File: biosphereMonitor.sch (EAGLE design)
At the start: 58 parts, among them IC1 XMEGA32A4AU, IC2 LM35, IC3 FT232RL, IC4 NE555D, IC5 SST25VF040, Q1 16Mhz, Q2 32kHz

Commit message: placed Parts
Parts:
- added C19: 4,7µF, rcl:CPOL-EUE2-5
- added R15: 10k, rcl:R-EU_R0805
- D1: value LM4050 2.5 -> 2.5
- JP5: value (none) -> BAT
- PH1: value BPW 96C TEL -> BPW 96
- renumbered BT! to BT1
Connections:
- net D+ renamed D_P
- net D- renamed D_N
- net N$9 renamed AVCC
- net USB_MC_D+ renamed USB_MC_D_P
- net USB_MC_D- renamed USB_MC_D_N
- new net N$28: IC3.!RESET, R15.2
- net +3V3: now also C19.+, R15.1
- net GND: now also C19.-
- net N$5: now also Q2.1; no longer Q2.2
- net N$6: now also Q2.2; no longer Q2.1
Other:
- moved on the sheet: Q2

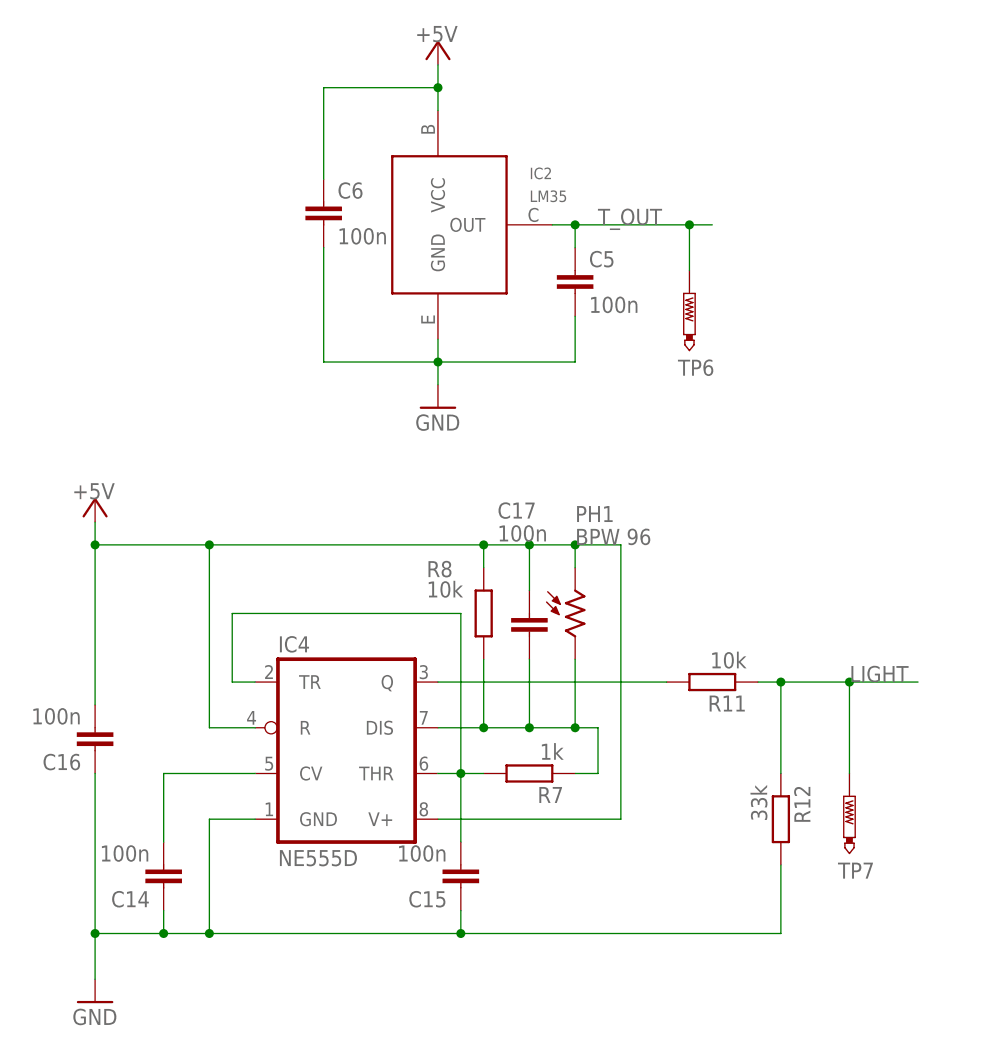
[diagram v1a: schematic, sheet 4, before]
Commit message: added PCB options and cam file
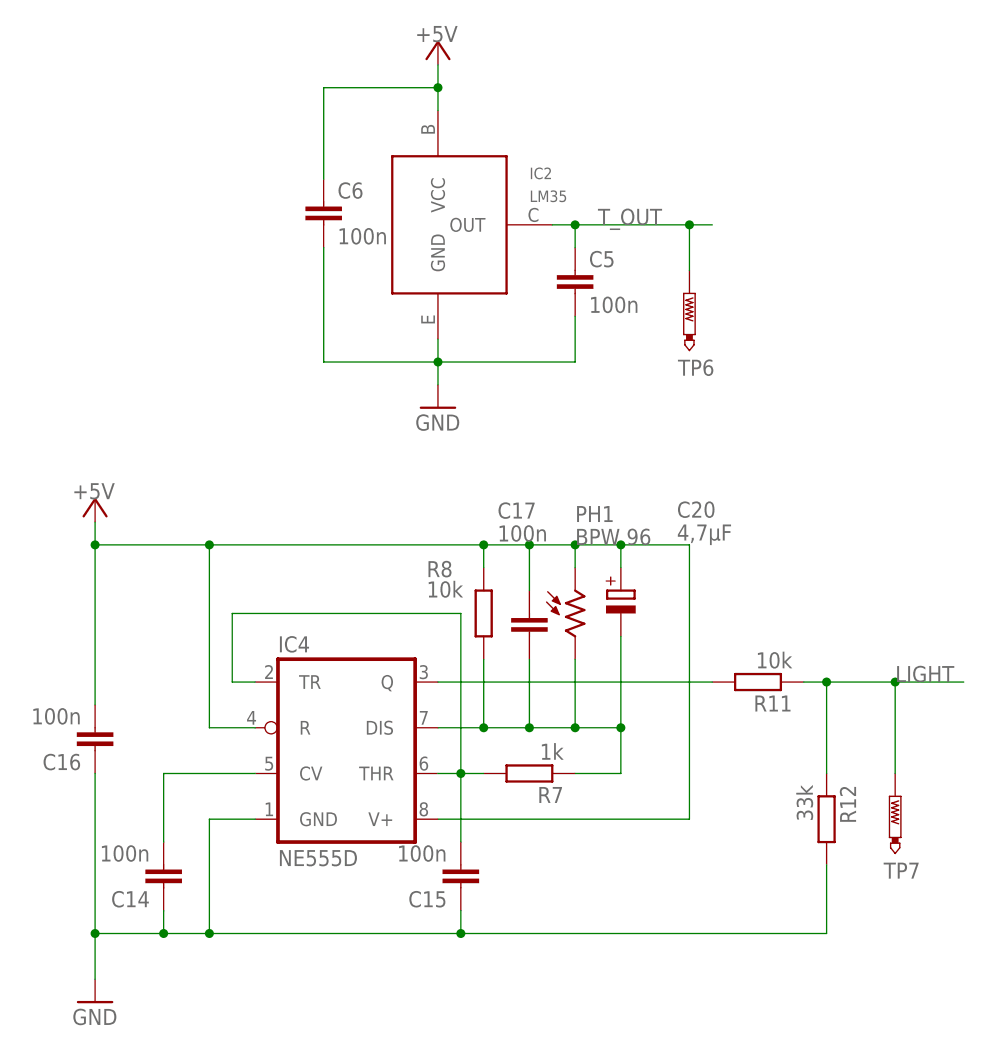
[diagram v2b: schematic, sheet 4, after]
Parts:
- added C20: 4,7µF, rcl:CPOL-EUE2-5
- added XIC6: 78L05F, linear:78L05F
- renumbered R15 to XR15, R2 to XR2, R3 to XR3
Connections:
- net +3V3: now also XIC6.VO
- net +5V: now also C20.+, XIC6.VI
- net GND: now also XIC6.GND, XIC6.GND@1
- net N$21: now also C20.-
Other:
- moved on the sheet: R11, R12, TP7

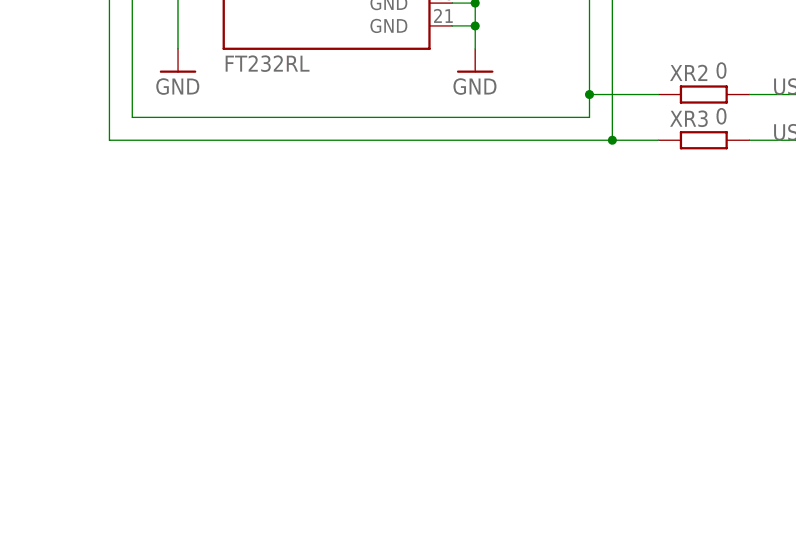
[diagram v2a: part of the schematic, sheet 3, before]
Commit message: added option for external ftdi board
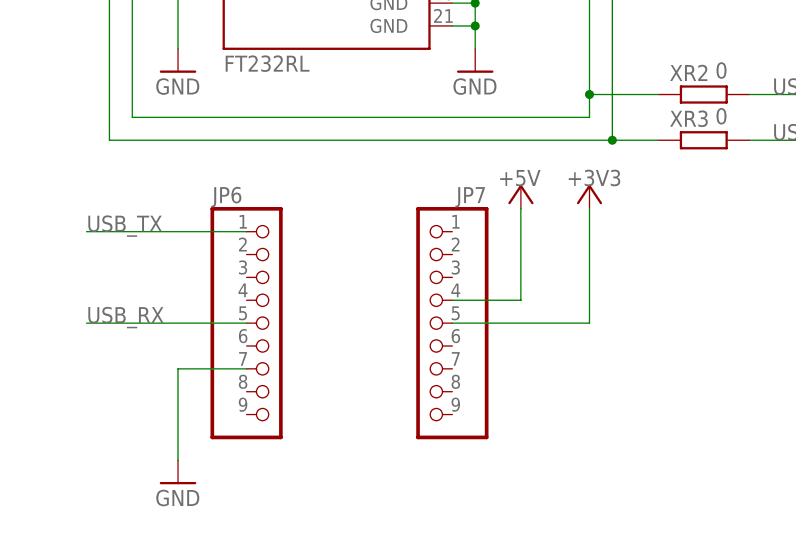
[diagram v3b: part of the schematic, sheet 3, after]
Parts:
- added JP6, JP7: (no value), pinhead:PINHD-1X9
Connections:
- net +3V3: now also JP7.5
- net +5V: now also JP7.4
- net GND: now also JP6.7
- net USB_RX: now also JP6.5
- net USB_TX: now also JP6.1
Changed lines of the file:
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@@
 <part name="GND19" library="supply1" library_urn="urn:adsk.eagle:library:371" deviceset="GND" device=""/>
 <part name="C20" library="rcl" library_urn="urn:adsk.eagle:library:334" deviceset="CPOL-EU" device="E2-5" package3d_urn="urn:adsk.eagle:package:23346/2" value="4,7µF"/>
+<part name="JP6" library="pinhead" library_urn="urn:adsk.eagle:library:325" deviceset="PINHD-1X9" device="" package3d_urn="urn:adsk.eagle:package:22483/2"/>
+<part name="JP7" library="pinhead" library_urn="urn:adsk.eagle:library:325" deviceset="PINHD-1X9" device="" package3d_urn="urn:adsk.eagle:package:22483/2"/>
+<part name="GND20" library="supply1" library_urn="urn:adsk.eagle:library:371" deviceset="GND" device=""/>
+<part name="+3V13" library="supply1" library_urn="urn:adsk.eagle:library:371" deviceset="+3V3" device=""/>
+<part name="P+10" library="supply1" library_urn="urn:adsk.eagle:library:371" deviceset="+5V" device=""/>
 </parts>
 <sheets>
@@
 <attribute name="VALUE" x="-33.02" y="27.94" size="1.778" layer="96"/>
 </instance>
+<instance part="JP6" gate="A" x="-5.08" y="-58.42" smashed="yes">
+<attribute name="NAME" x="-11.43" y="-45.085" size="1.778" layer="95"/>
+<attribute name="VALUE" x="-11.43" y="-73.66" size="1.778" layer="96"/>
+</instance>
+<instance part="JP7" gate="A" x="12.7" y="-58.42" smashed="yes" rot="MR0">
+<attribute name="NAME" x="19.05" y="-45.085" size="1.778" layer="95" rot="MR0"/>
+<attribute name="VALUE" x="19.05" y="-73.66" size="1.778" layer="96" rot="MR0"/>
+</instance>
+<instance part="GND20" gate="1" x="-15.24" y="-76.2" smashed="yes">
+<attribute name="VALUE" x="-17.78" y="-78.74" size="1.778" layer="96"/>
+</instance>
+<instance part="+3V13" gate="G$1" x="30.48" y="-43.18" smashed="yes">
+<attribute name="VALUE" x="27.94" y="-43.18" size="1.778" layer="96"/>
+</instance>
+<instance part="P+10" gate="1" x="22.86" y="-43.18" smashed="yes">
+<attribute name="VALUE" x="20.32" y="-43.18" size="1.778" layer="96"/>
+</instance>
 </instances>
 <busses>
@@
 <wire x1="-12.7" y1="20.32" x2="-30.48" y2="20.32" width="0.1524" layer="91"/>
 <junction x="-30.48" y="20.32"/>
+</segment>
+<segment>
+<pinref part="JP7" gate="A" pin="5"/>
+<pinref part="+3V13" gate="G$1" pin="+3V3"/>
+<wire x1="15.24" y1="-58.42" x2="30.48" y2="-58.42" width="0.1524" layer="91"/>
+<wire x1="30.48" y1="-58.42" x2="30.48" y2="-45.72" width="0.1524" layer="91"/>
 </segment>
 </net>
@@
 <wire x1="53.34" y1="-5.08" x2="50.8" y2="-5.08" width="0.1524" layer="91"/>
 </segment>
+<segment>
+<pinref part="GND20" gate="1" pin="GND"/>
+<pinref part="JP6" gate="A" pin="7"/>
+<wire x1="-15.24" y1="-73.66" x2="-15.24" y2="-63.5" width="0.1524" layer="91"/>
+<wire x1="-15.24" y1="-63.5" x2="-7.62" y2="-63.5" width="0.1524" layer="91"/>
+</segment>
 </net>
 <net name="USB_TX" class="0">
@@
 <pinref part="IC3" gate="1" pin="TXD"/>
 </segment>
+<segment>
+<pinref part="JP6" gate="A" pin="1"/>
+<wire x1="-7.62" y1="-48.26" x2="-25.4" y2="-48.26" width="0.1524" layer="91"/>
+<label x="-25.4" y="-48.26" size="1.778" layer="95"/>
+</segment>
 </net>
 <net name="USB_RX" class="0">
@@
 <pinref part="IC3" gate="1" pin="RXD"/>
 </segment>
+<segment>
+<pinref part="JP6" gate="A" pin="5"/>
+<wire x1="-7.62" y1="-58.42" x2="-25.4" y2="-58.42" width="0.1524" layer="91"/>
+<label x="-25.4" y="-58.42" size="1.778" layer="95"/>
+</segment>
 </net>
 <net name="+5V" class="0">
@@
 <pinref part="IC3" gate="1" pin="VCC"/>
 </segment>
-</net>
+<segment>
+<pinref part="JP7" gate="A" pin="4"/>
+<pinref part="P+10" gate="1" pin="+5V"/>
+<wire x1="15.24" y1="-55.88" x2="22.86" y2="-55.88" width="0.1524" layer="91"/>
+<wire x1="22.86" y1="-55.88" x2="22.86" y2="-45.72" width="0.1524" layer="91"/>
+</segment>
+</net>

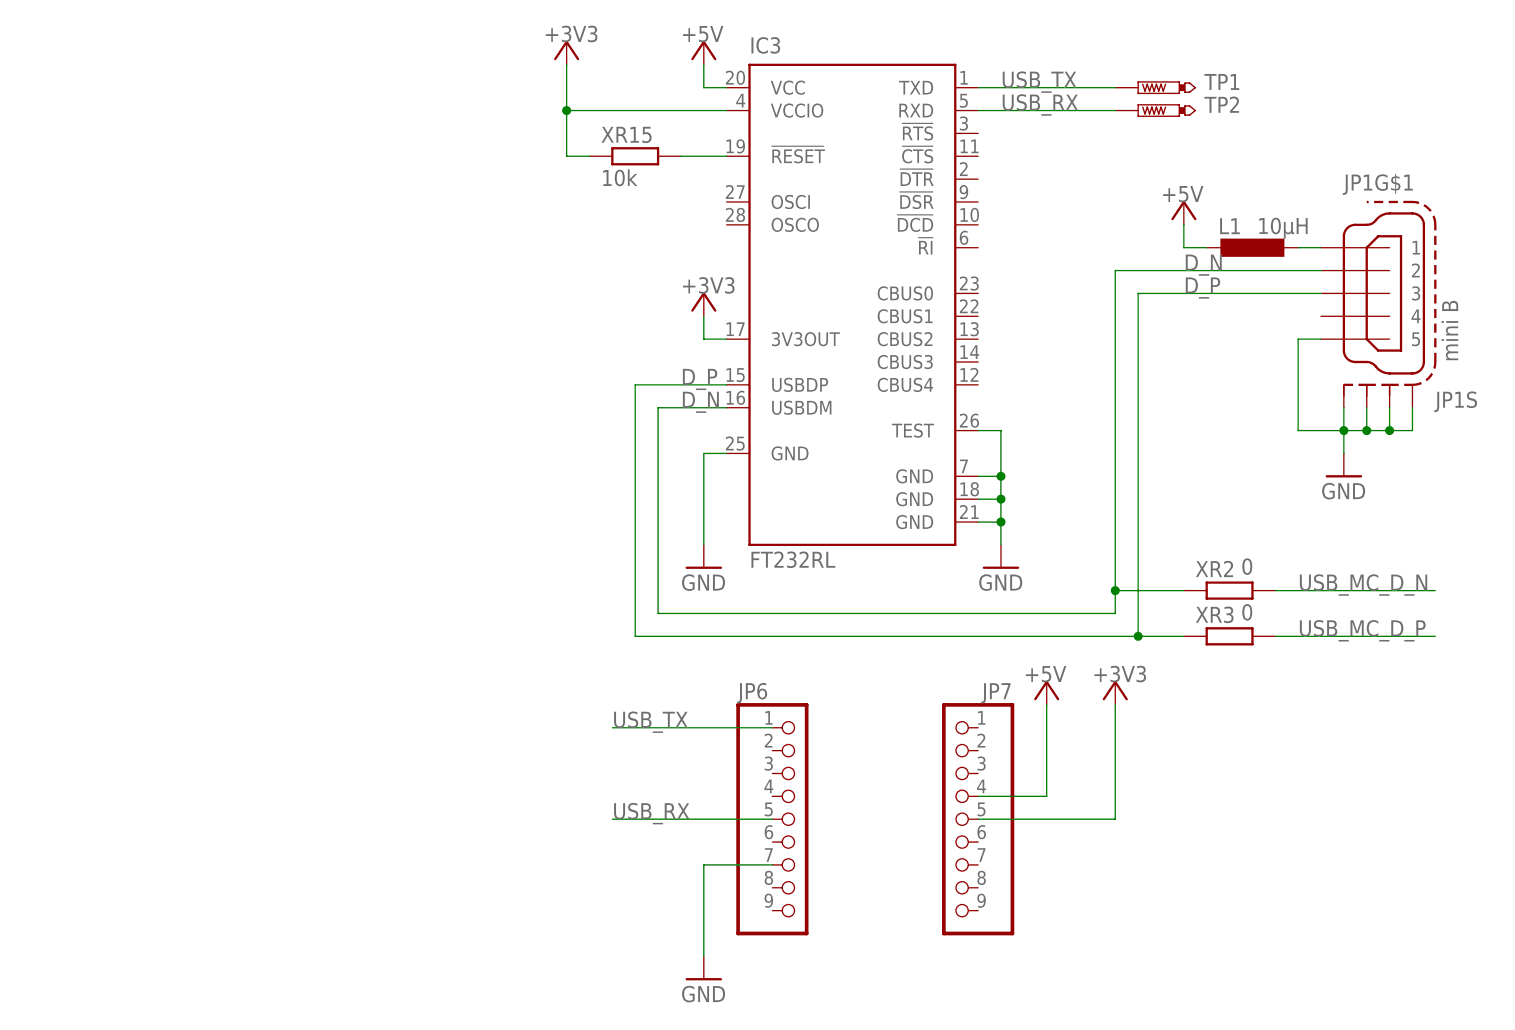
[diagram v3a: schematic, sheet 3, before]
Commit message: changed some footprints
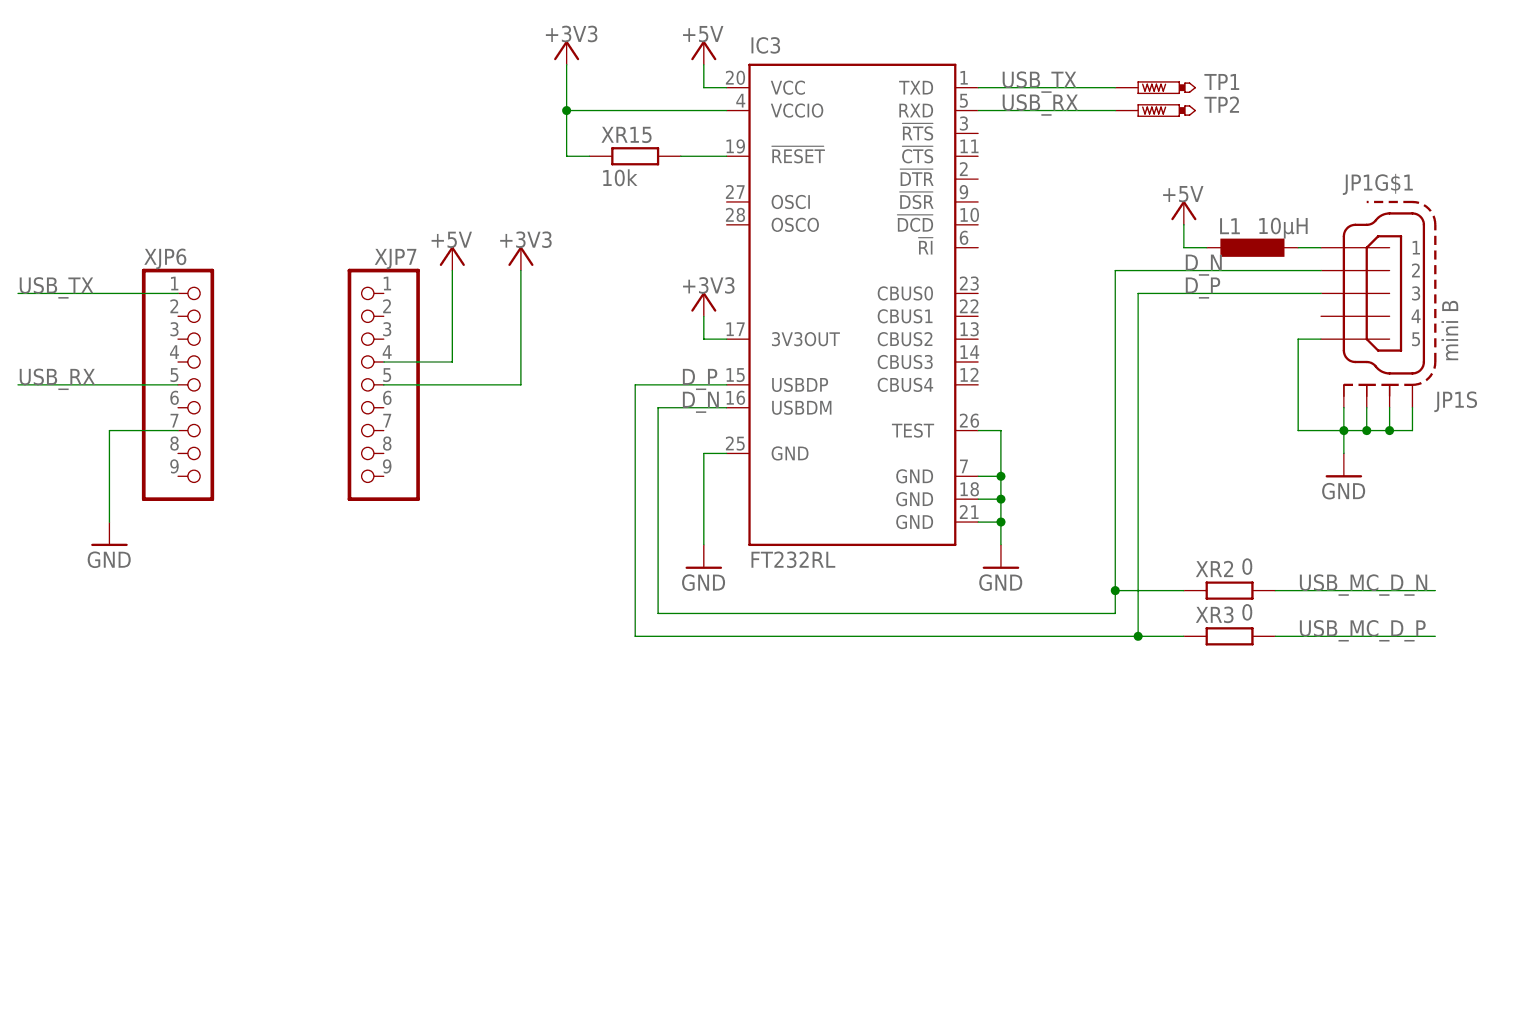
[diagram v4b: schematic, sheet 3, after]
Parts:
- removed JP6, JP7: (no value), pinhead:PINHD-1X9
- added XJP6, XJP7: (no value), pinhead:PINHD-1X9
- C13, C19, C20: value 4,7µF -> 220µ; device rcl:CPOL-EUE2-5 -> rcl:CPOL-EUG
- Q1: device crystal:CRYSTALHC49UP -> crystal:CRYSTALSM49
- Q2: device crystal:CRYSTALTC38H -> Tjarks_Bauteile (1):MQ_CRYSTALMS1V
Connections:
- net +3V3: now also XJP7.5; no longer JP7.5
- net +5V: now also XJP7.4; no longer JP7.4
- net GND: now also XJP6.7; no longer JP6.7
- net USB_RX: now also XJP6.5; no longer JP6.5
- net USB_TX: now also XJP6.1; no longer JP6.1

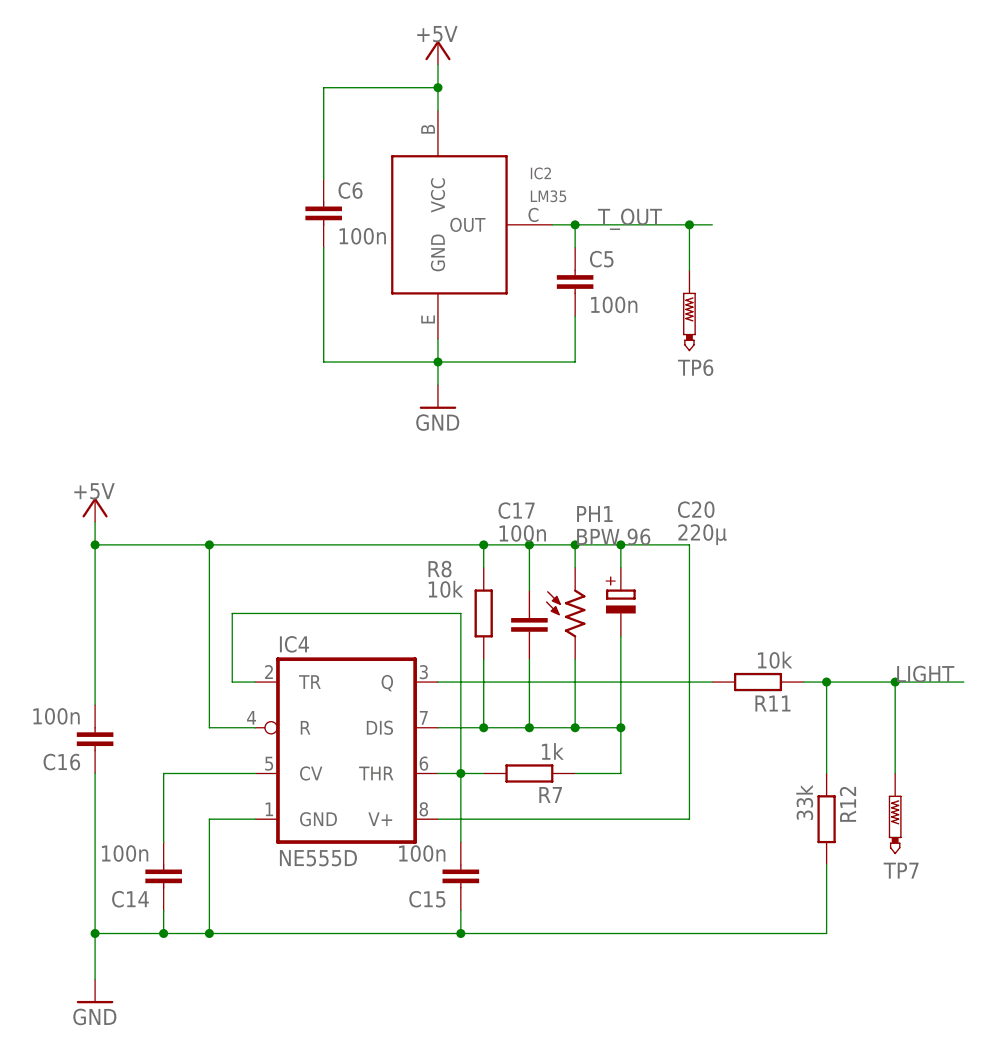
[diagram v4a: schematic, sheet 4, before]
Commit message: removed unnecesary parts
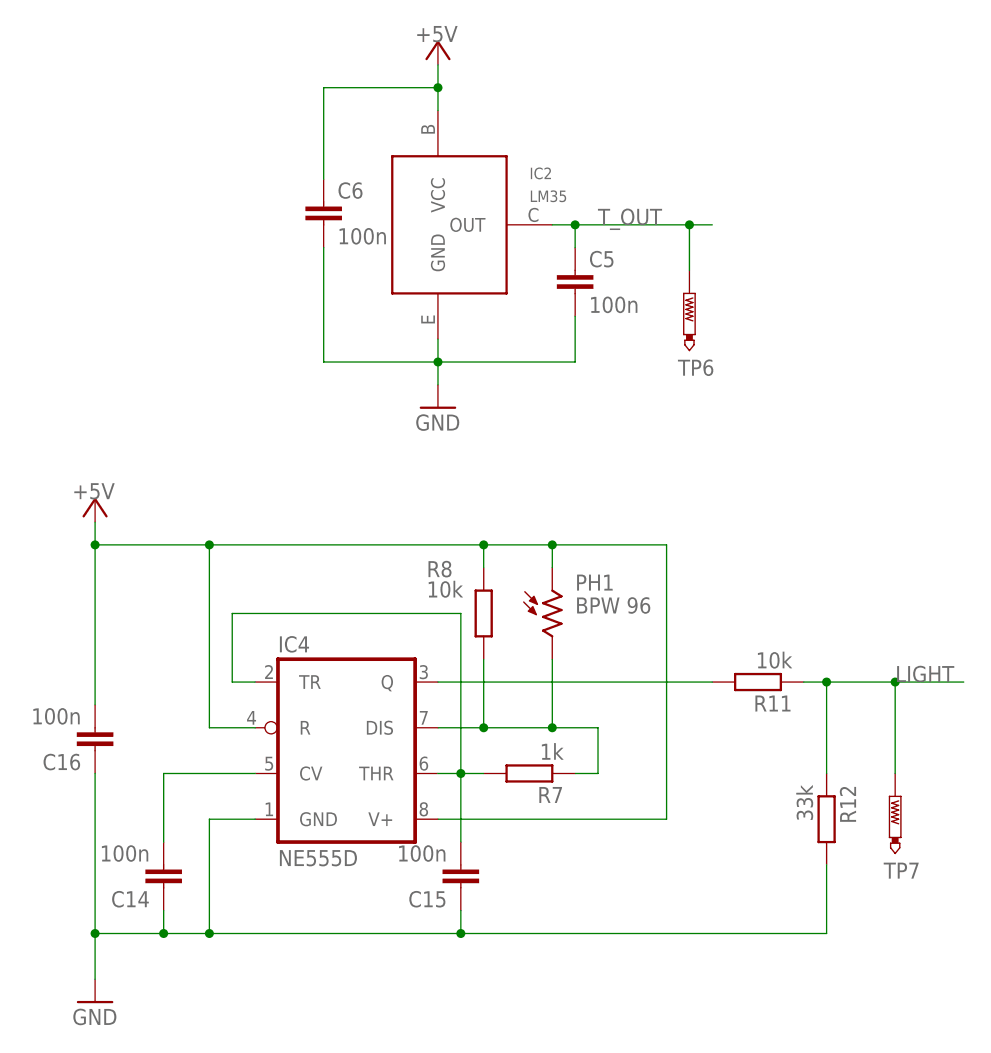
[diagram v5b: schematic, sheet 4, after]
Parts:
- removed C17: 100n, rcl:C-EUC0805
- removed C20: 220µ, rcl:CPOL-EUG
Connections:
- net +5V: no longer C17.1, C20.+
- net N$21: no longer C17.2, C20.-
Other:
- moved on the sheet: PH1
